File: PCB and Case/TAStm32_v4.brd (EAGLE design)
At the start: 50 x 100 mm, 47 parts, among them IC1 74AVCH4T245PW,118, IC2 74AVCH4T245PW,118, IC3 74AVCH4T245PW,118, J1 ZX62D-B-5PA8, J10 RJSSE538002, J11 RJSSE538002, J12 SOICBITE, J13 CONSOLE_RESET, J2 UE27-AC54-100, J3 TSM-105-02-L-SHJ, J4 CONSOLE_RESET, J5 OLED128X64, J6 SAMTEC-TSM-116-01-X-SVJ, J7 SAMTEC-TSM-116-01-X-SVJ, U1 STM32F446RET6, U2 3.3V REG, Y1 8MHz

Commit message: more new buffers
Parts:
- removed C15, C16, C19: 100nF, rcl:C0603K
- removed IC1, IC2, IC3: 74AVCH4T245PW,118, SamacSys_Parts:SOP65P640X110-16N
- removed RN3: CTS742C083, resistor-net:CTS742C083
- added IC4: 74LVC14, 74xx-us:SO14
- added IC5: 74HCT125, 74xx-eu:TSSOP14
- added IC7: 74LVC07, 74xx-us:SO14
- added RN4, RN5: CTS742C083, resistor-net:CTS742C083
- moved RN2 145.3 mm to (-9.75, -71.5)
- moved RN1 142.2 mm to (-9.75, -64.8)
- moved C13 132.5 mm to (-10.5, -54.7), turned to 0 degrees
- moved C14 126.5 mm to (-10.5, -59.1), turned to 0 degrees
- moved C5 123.6 mm to (-10.5, -50.3), turned to 0 degrees
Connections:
- removed net N$10: IC2.10, RN2.4
- removed net N$11: IC2.13, RN2.1
- removed net N$12: IC1.12, RN3.2
- removed net N$13: IC1.11, RN3.3
- removed net N$14: IC1.10, RN3.4
- removed net N$15: IC1.13, RN3.1
- removed net N$4: IC3.11, RN1.3
- removed net N$6: IC3.10, RN1.4
- removed net N$8: IC2.12, RN2.2
- removed net N$9: IC2.11, RN2.3
- removed net P1_5V: C13.2, C15.2, D1.A, IC1.16, IC3.16, J10.10, J6.10
- removed net P2_5V: C5.2, D2.A, IC2.16, J10.2, J6.2
- new net GND1: C13.1
- new net N$16: IC4.13, RN1.1, RN4.8
- new net N$17: IC4.11, RN1.2, RN4.7
- new net N$18: IC4.9, RN1.3, RN4.6
- new net N$21: IC4.5, RN2.3, RN5.6
- new net OUTPUTS_ENABLE: IC5.1, IC5.10, IC5.13, IC5.4
- new net P1_D2_3V_IN: IC4.8
- new net P1_VCC: D1.A, J10.10, J6.10
- new net P2_D3_3V_IN: IC4.6
- new net P2_VCC: D2.A, J10.2, J6.2
- new net V+1: C14.2, IC5.14
- net DIR_CLKLAT: no longer IC1.3, IC2.3
- net DIR_D0D1: no longer IC1.2, IC2.2
- net DIR_P1D2D3: no longer IC3.2
- net DIR_P2D2D3: no longer IC3.3
- net ENABLE_CLKLAT: no longer IC1.14, IC2.14
- net ENABLE_D0D1: no longer IC1.15, IC2.15
- net ENABLE_P1D2D3: no longer IC3.15
- net ENABLE_P2D2D3: no longer IC3.14
- net GND: now also IC4.7, IC5.7, IC7.11, IC7.13, IC7.7; no longer C13.1, C15.1, C16.1, C19.1, IC1.8, IC1.9, IC2.8, IC2.9, IC3.8, IC3.9
- net N$2: now also IC4.1, RN2.1, RN5.8; no longer IC3.13, RN1.1
- net N$3: now also IC4.3, RN2.2, RN5.7; no longer IC3.12, RN1.2
- net P1_CLOCK: now also RN4.2; no longer RN3.5
- net P1_CLOCK_3V: now also IC4.10; no longer IC1.7
- net P1_D0: now also IC5.3; no longer RN3.8
- net P1_D0_3V: now also IC5.2; no longer IC1.4
- net P1_D1: now also IC5.6; no longer RN3.7
- net P1_D1_3V: now also IC5.5; no longer IC1.5
- net P1_D2: now also IC7.2, RN4.3; no longer RN1.5
- net P1_D2_3V: now also IC7.1; no longer IC3.7
- net P1_D3: now also IC7.4; no longer RN1.6
- net P1_D3_3V: now also IC7.3; no longer IC3.6
- net P1_LATCH: now also RN4.1; no longer RN3.6
- net P1_LATCH_3V: now also IC4.12; no longer IC1.6
- net P2_CLOCK: now also RN5.2; no longer RN2.5
- net P2_CLOCK_3V: now also IC4.4; no longer IC2.7
- net P2_D0: now also IC5.8; no longer RN2.8
- net P2_D0_3V: now also IC5.9; no longer IC2.4
- net P2_D1: now also IC5.11; no longer RN2.7
- net P2_D1_3V: now also IC5.12; no longer IC2.5
- net P2_D2: now also IC7.6; no longer RN1.8
- net P2_D2_3V: now also IC7.5; no longer IC3.4
- net P2_D3: now also IC7.8, RN5.3; no longer RN1.7
- net P2_D3_3V: now also IC7.9; no longer IC3.5
- net P2_LATCH: now also RN5.1; no longer RN2.6
- net P2_LATCH_3V: now also IC4.2; no longer IC2.6
- net V+: now also C13.2, C5.2, IC4.14, IC7.14, RN1.6, RN1.7, RN1.8, RN2.6, RN2.7, RN2.8; no longer C14.2, C16.2, C19.2, IC1.1, IC2.1, IC3.1
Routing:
- net P1_5V: track 65.2 -> 0.00 mm, vias 4 -> 0
- net P1_VCC: track 0.00 -> 54.8 mm, vias 0 -> 2
- net P2_5V: track 51.7 -> 0.00 mm
- net P2_VCC: track 0.00 -> 43.6 mm
- net DIR_D0D1: track 39.5 -> 21.2 mm, vias 2 -> 0
- net DIR_CLKLAT: track 38.7 -> 21.5 mm
- net GND: track 134.3 -> 118.2 mm, vias 65 -> 52
- net V+: track 264.8 -> 258.0 mm
- net N$15: track 5.77 -> 0.00 mm
- net N$12: track 5.62 -> 0.00 mm
- net N$13: track 5.57 -> 0.00 mm
- net N$14: track 5.50 -> 0.00 mm
- net N$3: track 4.29 -> 0.00 mm
- net P2_CLOCK_3V: track 18.8 -> 14.7 mm
- net N$4: track 4.05 -> 0.00 mm
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
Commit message: bleh updates
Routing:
- net ENABLE_CLKLAT: track 47.0 -> 11.1 mm, vias 2 -> 0
- net V+: track 258.0 -> 228.0 mm, vias 13 -> 9
- net ENABLE_D0D1: track 42.1 -> 14.7 mm, vias 2 -> 0
- net ENABLE_P2D2D3: track 25.6 -> 8.01 mm, vias 2 -> 0
- net ENABLE_P1D2D3: track 25.7 -> 8.22 mm, vias 2 -> 0
- net P2_D3_3V: track 20.1 -> 8.42 mm
- net P1_D3_3V: track 18.9 -> 8.63 mm
- net P2_LATCH_3V: track 20.8 -> 12.0 mm, vias 2 -> 0
- net GND: track 118.2 -> 109.3 mm, vias 52 -> 40
- net DIR_P2D2D3: track 14.7 -> 6.36 mm
- net DIR_P1D2D3: track 14.2 -> 6.56 mm
- net P2_D0_3V: track 20.5 -> 13.0 mm, vias 2 -> 0
- net P2_D1_3V: track 19.0 -> 12.5 mm
- net P1_D2_3V: track 14.7 -> 8.84 mm
- net P2_CLOCK_3V: track 14.7 -> 9.07 mm, vias 2 -> 0
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
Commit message: more code work
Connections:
- net P2_D3_3V_IN renamed P2_D2_3V_IN
- net OUTPUTS_ENABLE: now also RN2.4
- net V+: now also RN2.5
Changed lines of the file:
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@@
 <contactref element="RN2" pad="7"/>
 <contactref element="RN2" pad="6"/>
+<contactref element="RN2" pad="5"/>
 <wire x1="-10.1536" y1="-70.6756" x2="-10.9536" y2="-70.6756" width="0" layer="19" extent="1-1"/>
 <wire x1="-9.3536" y1="-70.6756" x2="-10.1536" y2="-70.6756" width="0" layer="19" extent="1-1"/>
+<wire x1="-8.5536" y1="-70.6756" x2="-9.3536" y2="-70.6756" width="0" layer="19" extent="1-1"/>
 <wire x1="-10.9536" y1="-63.97" x2="-10.9536" y2="-70.6756" width="0" layer="19" extent="1-1"/>
 <wire x1="-10.1536" y1="-63.97" x2="-10.9536" y2="-63.97" width="0" layer="19" extent="1-1"/>
@@
 <contactref element="IC4" pad="8"/>
 </signal>
-<signal name="P2_D3_3V_IN">
+<signal name="P2_D2_3V_IN">
 <contactref element="IC4" pad="6"/>
 </signal>
@@
 <contactref element="IC5" pad="4"/>
 <contactref element="IC5" pad="1"/>
+<contactref element="RN2" pad="4"/>
+<wire x1="-9.2652" y1="-30.357" x2="-8.5536" y2="-72.2756" width="0" layer="19" extent="1-1"/>
 <wire x1="-7.3152" y1="-30.357" x2="-9.2652" y2="-30.357" width="0" layer="19" extent="1-1"/>
 <wire x1="-8.6152" y1="-24.507" x2="-9.2652" y2="-30.357" width="0" layer="19" extent="1-1"/>

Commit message: caps
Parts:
- added CN1, CN2: CA0612KRX7R7BB104, SamacSys_Parts:CA0612KRX7R7BB104
- added RN3: CTS742C083, resistor-net:CTS742C083
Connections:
- removed net N$21: IC4.5, RN2.3, RN5.6
- new net N$4: CN2.8, IC4.1, RN2.1, RN5.8
- new net N$6: CN2.7, IC4.3, RN2.2, RN5.7
- new net N$8: CN2.6, IC4.5, RN2.3, RN5.6
- net GND: now also CN1.1, CN1.2, CN1.3, CN1.4, CN2.1, CN2.2, CN2.3, CN2.4
- net N$16: now also CN1.8
- net N$17: now also CN1.7
- net N$18: now also CN1.6
- net N$2: now also IC5.6, RN3.2; no longer IC4.1, RN2.1, RN5.8
- net N$3: now also IC5.3, RN3.1; no longer IC4.3, RN2.2, RN5.7
- net P1_D0: now also RN3.8; no longer IC5.3
- net P1_D1: now also RN3.7; no longer IC5.6
- net P1_D2: now also RN3.6; no longer IC7.2
- net P1_D3: now also RN3.5; no longer IC7.4

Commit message: new new new new buffers
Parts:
- removed IC5: 74HCT125, 74xx-eu:TSSOP14
- removed IC7: 74LVC07, 74xx-us:SO14
- added C15, C16, C17: 100nF, rcl:C0603K
- added CN3, CN4: CA0612KRX7R7BB104, SamacSys_Parts:CA0612KRX7R7BB104
- added IC1, IC2: 74HCT3G07DP-Q100H, SamacSys_Parts:SOP65P400X110-8N
- added IC3: 74AVCH4T245PW,118, SamacSys_Parts:SOP65P640X110-16N
- added RN7: CTS742C083, resistor-net:CTS742C083
- IC4: value 74LVC14 -> 74AVCH4T245PW,118; device 74xx-us:SO14 -> SamacSys_Parts:SOP65P640X110-16N
- moved RN3 170.9 mm to (53.8, 68.4)
- moved CN2 161.5 mm to (53.5, 67.5), turned to 90 degrees
- moved RN1 154.2 mm to (57.5, 74.1)
- moved C5 152.1 mm to (58.1, 85.5)
- moved RN2 144.4 mm to (38.6, 64.6)
- moved CN1 143.9 mm to (47.7, 61.9), turned to 270 degrees
- moved C13 143.5 mm to (62.9, 68.6)
- moved C14 143.5 mm to (62.9, 64.2)
- moved RN5 97.1 mm to (42.8, 62.0)
- moved RN4 94.0 mm to (38.4, 67.8)
- moved IC4 74.7 mm to (32.5, 59.0), turned to 90 degrees
- moved C3 2.12 mm to (47.2, 36.0)
- moved C1 2.00 mm to (35.0, 45.9)
- moved C11 2.00 mm to (45.8, 40.3)
- moved C12 2.00 mm to (45.8, 42.1)
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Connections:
- removed net DIR_CLKLAT: U1.14
- removed net ENABLE_CLKLAT: U1.29
- removed net GND1: C13.1
- removed net OUTPUTS_ENABLE: IC5.1, IC5.10, IC5.13, IC5.4, RN2.4
- removed net P1_D2_3V: IC7.1, U1.24
- removed net P2_D2_3V: IC7.5, U1.40
- removed net V+1: C14.2, IC5.14
- new net N$10: IC3.10, RN3.4
- new net N$11: IC4.12, RN7.2
- new net N$12: IC4.13, RN7.1
- new net N$13: IC4.11, RN7.3
- new net N$14: IC4.10, RN7.4
- new net N$9: IC3.11, RN3.3
- new net P1_D2_3V_OUT: IC3.4, U1.15
- new net P2_D2_3V_OUT: IC4.6
- net DIR_D0D1: now also IC3.3, IC4.2, U1.16; no longer U1.15
- net DIR_P1D2D3: now also IC3.2, U1.20; no longer U1.27
- net DIR_P2D2D3: now also IC4.3
- net ENABLE_D0D1: now also IC3.14, IC4.15, U1.21; no longer U1.16
- net ENABLE_P1D2D3: now also IC3.15, U1.22; no longer U1.21
- net ENABLE_P2D2D3: now also IC4.14; no longer U1.20
- net GND: now also C13.2, C15.2, C16.1, C17.2, C5.2, CN3.1, CN3.2, CN3.3, CN3.4, CN4.1, CN4.2, CN4.3, CN4.4, IC1.4, IC2.4, IC3.8, IC3.9, IC4.8, IC4.9; no longer C5.1, IC4.7, IC5.7, IC7.11, IC7.13, IC7.7
- net N$16: now also IC1.1; no longer IC4.13
- net N$17: now also IC1.6; no longer IC4.11
- net N$18: now also IC1.3; no longer IC4.9
- net N$2: now also IC3.12; no longer IC5.6
- net N$3: now also IC3.13; no longer IC5.3
- net N$4: now also IC2.1; no longer IC4.1
- net N$6: now also IC2.6; no longer IC4.3
- net N$8: now also IC2.3; no longer IC4.5
- net P1_CLOCK_3V: now also IC1.2; no longer IC4.10
- net P1_D0: now also CN3.8
- net P1_D0_3V: now also IC3.6; no longer IC5.2
- net P1_D1: now also CN3.5
- net P1_D1_3V: now also IC3.7; no longer IC5.5
- net P1_D2_3V_IN: now also IC1.5, U1.24; no longer IC4.8
- net P1_D3_3V: now also IC3.5, U1.14; no longer IC7.3
- net P1_LATCH_3V: now also IC1.7; no longer IC4.12
- net P1_VCC: now also C15.1, C17.1, IC3.16, IC4.16
- net P2_CLOCK_3V: now also IC2.2; no longer IC4.4
- net P2_D0: now also CN4.5, RN7.7; no longer IC5.8
- net P2_D0_3V: now also IC4.5; no longer IC5.9
- net P2_D1: now also CN4.8, RN7.8; no longer IC5.11
- net P2_D1_3V: now also IC4.4; no longer IC5.12
- net P2_D2: now also RN5.3, RN7.6; no longer IC7.6
- net P2_D2_3V_IN: now also IC2.5, U1.40; no longer IC4.6
- net P2_D3: now also RN7.5; no longer IC7.8, RN5.3
- net P2_D3_3V: now also IC4.7, U1.27; no longer IC7.9, U1.22
- net P2_LATCH_3V: now also IC2.7; no longer IC4.2
- net V+: now also C13.1, C14.2, C16.2, C5.1, IC1.8, IC2.8, IC3.1, IC4.1; no longer C13.2, C5.2, IC4.14, IC7.14
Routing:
- net P2_LATCH_3V: track 12.0 -> 33.1 mm
- net P2_D2_3V: track 20.0 -> 0.00 mm, vias 2 -> 0
- net SWITCH3: track 23.8 -> 5.94 mm
- net P1_D3_3V: track 8.63 -> 25.9 mm
- net P1_D2_3V_OUT: track 0.00 -> 16.8 mm
- net DIR_CLKLAT: track 16.5 -> 0.00 mm
- net DIR_P2D2D3: track 6.36 -> 22.5 mm
- net P2_D2_3V_IN: track 0.00 -> 11.2 mm
- net ENABLE_CLKLAT: track 11.1 -> 0.00 mm
- net ENABLE_P1D2D3: track 8.22 -> 18.3 mm
- net P1_D2_3V_IN: track 0.00 -> 8.84 mm
- net P1_D2_3V: track 8.84 -> 0.00 mm
- net P2_D1_3V: track 12.5 -> 20.8 mm
- net P2_D0_3V: track 13.0 -> 21.2 mm
- net P2_D3_3V: track 8.42 -> 15.8 mm
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
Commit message: new buffer funtimes
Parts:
- moved C16 35.1 mm to (41.3, 50.1), turned to 90 degrees
- moved C13 26.9 mm to (37.9, 58.5)
- moved C15 22.0 mm to (41.0, 61.6), turned to 90 degrees
- moved C14 19.5 mm to (47.7, 52.0)
- moved RN1 16.2 mm to (47.9, 61.0)
- moved CN2 15.7 mm to (38.0, 65.0), turned to 270 degrees
- moved RN3 12.3 mm to (43.6, 61.6)
- moved CN3 11.4 mm to (43.6, 65.1), turned to 270 degrees
- moved CN4 9.84 mm to (33.1, 68.6), turned to 270 degrees
- moved RN4 9.33 mm to (47.7, 68.6), turned to 180 degrees
- moved RN5 7.92 mm to (38.0, 68.3), turned to 180 degrees
- moved RN2 3.12 mm to (38.0, 61.5)
- moved CN1 2.74 mm to (47.7, 64.6)
- moved IC2 1.07 mm to (38.0, 54.9)
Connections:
- net N$16: now also RN1.3; no longer RN1.1
- net N$17: now also RN1.1; no longer RN1.2
- net N$18: now also RN1.2; no longer RN1.3
- net N$4: now also CN2.6, RN2.2, RN5.6; no longer CN2.8, RN2.1, RN5.8
- net N$6: now also CN2.5, RN2.1, RN5.5; no longer CN2.7, RN2.2, RN5.7
- net N$8: now also CN2.8, RN2.4, RN5.8; no longer CN2.6, RN2.3, RN5.6
- net P1_D0: now also CN3.7, RN3.6; no longer CN3.8, RN3.8
- net P1_D1: now also CN3.8, RN3.5; no longer CN3.5, RN3.7
- net P1_D2: now also RN3.8; no longer RN3.6
- net P1_D3: now also RN3.7; no longer RN3.5
- net P1_D3_3V: no longer U1.23
- net P1_VCC: no longer C17.1, IC4.16
- net P2_D0: now also CN4.8; no longer CN4.5
- net P2_D1: now also CN4.5; no longer CN4.8
- net P2_VCC: now also C17.1, IC4.16
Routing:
- net N$4: track 0.00 -> 22.0 mm
- net P2_D2_3V_IN: track 11.2 -> 28.9 mm, vias 0 -> 2
- net N$8: track 0.00 -> 17.0 mm
- net P2_D0: track 30.0 -> 45.9 mm
- net N$6: track 0.00 -> 13.8 mm
- net P1_VCC: track 51.3 -> 37.7 mm, vias 2 -> 0
- net P1_D2_3V_IN: track 8.84 -> 22.3 mm, vias 0 -> 2
- net P1_D0: track 18.4 -> 27.3 mm
- net P1_D3_3V: track 25.9 -> 17.3 mm
- net P1_D1: track 18.3 -> 26.8 mm
- net P1_D2: track 19.6 -> 27.9 mm
- net P2_LATCH: track 25.7 -> 33.6 mm, vias 0 -> 2
- net P2_LATCH_3V: track 33.1 -> 25.7 mm
- net V+: track 221.2 -> 227.7 mm
- net P1_LATCH: track 17.6 -> 11.4 mm
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
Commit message: no airwires!
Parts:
- CN1, CN2, CN3, CN4: value CA0612KRX7R7BB104 -> 330pF
- RN1, RN2, RN5: value CTS742C083 -> 47K
- RN4, RN7: value CTS742C083 -> 47R
- moved C5 40.8 mm to (31.2, 54.7)
- moved C17 35.9 mm to (30.2, 65.2), turned to 90 degrees
- moved RN5 0.61 mm to (38.0, 68.9)
- moved IC4 0.55 mm to (33.0, 59.3)
- moved CN3 0.46 mm to (43.1, 65.1)
- moved C14 0.34 mm to (47.4, 51.8)
- moved IC1 0.30 mm to (47.7, 56.0)
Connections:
- removed net N$13: IC4.11, RN7.3
- removed net N$14: IC4.10, RN7.4
- removed net N$2: IC3.12, RN3.2
- removed net N$3: IC3.13, RN3.1
- net ENABLE_P2D2D3: now also U1.23
- net N$16: now also CN1.7, RN4.7; no longer CN1.8, RN4.8
- net N$17: now also CN1.5, RN4.5; no longer CN1.7, RN4.7
- net P1_CLOCK: now also RN4.4; no longer RN4.2
- net P1_D2: now also IC3.13, RN3.1
- net P1_D3: now also IC3.12, RN3.2
- net P1_LATCH: now also RN4.2; no longer RN4.1
- net P1_VCC: now also RN1.5, RN1.6, RN1.7, RN1.8
- net P2_CLOCK: now also RN5.4; no longer RN5.2
- net P2_D2: now also IC4.11, RN5.1, RN7.3; no longer RN5.3
- net P2_D2_3V_OUT: now also U1.29
- net P2_D3: now also IC4.10, RN7.4
- net P2_LATCH: now also RN5.3; no longer RN5.1
- net P2_VCC: now also RN2.5, RN2.6, RN2.7, RN2.8
- net V+: no longer RN1.6, RN1.7, RN1.8, RN2.5, RN2.6, RN2.7, RN2.8
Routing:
- net V+: track 227.7 -> 281.0 mm, vias 9 -> 15
- net P1_VCC: track 37.7 -> 84.0 mm, vias 0 -> 4
- net P1_D2: track 27.9 -> 59.1 mm
- net GND: track 103.1 -> 133.7 mm, vias 34 -> 52
- net P1_LATCH: track 11.4 -> 38.5 mm
- net P2_VCC: track 43.6 -> 68.6 mm, vias 0 -> 2
- net ENABLE_P2D2D3: track 4.90 -> 27.4 mm, vias 0 -> 4
- net DIR_D0D1: track 16.2 -> 38.4 mm, vias 0 -> 4
- net SWITCH3: track 5.94 -> 23.3 mm
- net P2_D2_3V_OUT: track 0.00 -> 17.0 mm
- net ENABLE_D0D1: track 18.3 -> 34.0 mm, vias 0 -> 2
- net NRST: track 68.0 -> 82.8 mm, vias 2 -> 4
- net N$16: track 2.48 -> 14.3 mm
- net N$18: track 2.28 -> 13.9 mm
- net P2_D2: track 43.0 -> 54.3 mm, vias 0 -> 2
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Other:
- board text added: "TAStm32"
- board text added: "v4 rev2"
- board text removed: "TAStm32 v4 rev2"

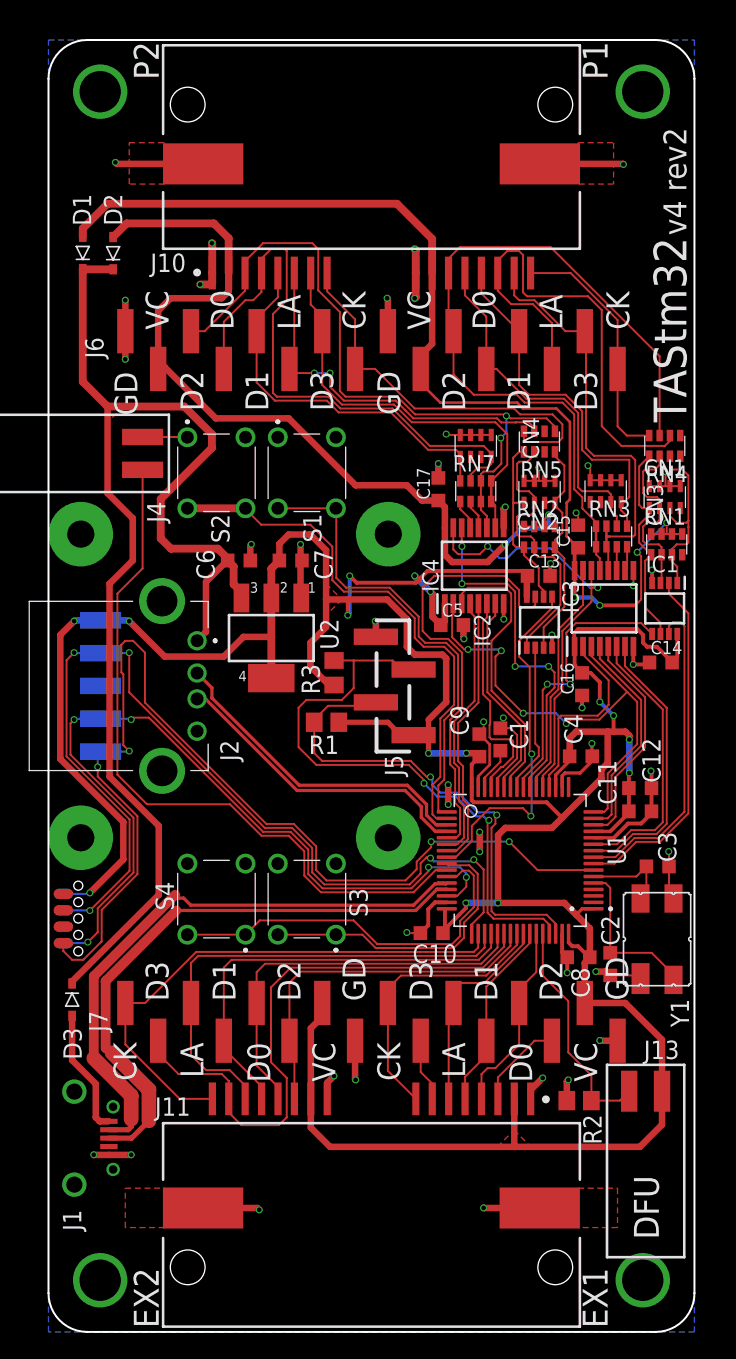
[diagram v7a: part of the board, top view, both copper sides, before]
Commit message: v4 r2 silkscreen cleanup, combi vis board
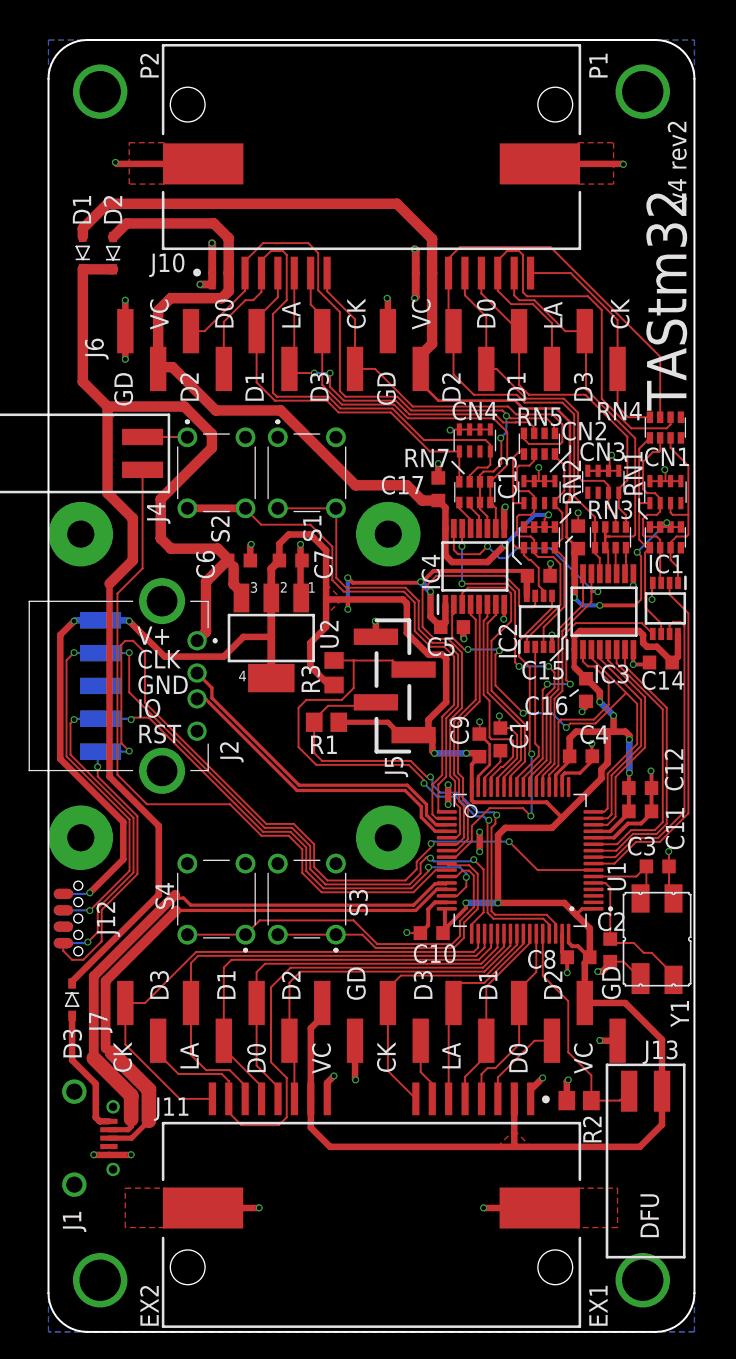
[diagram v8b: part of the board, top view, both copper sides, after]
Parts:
- moved RN4 1.42 mm to (47.8, 70.0)
- moved C2 1.07 mm to (43.5, 29.5)
- moved CN3 0.75 mm to (42.9, 65.8)
- moved RN1 0.55 mm to (47.8, 61.5)
- moved C16 0.55 mm to (41.6, 49.7)
- moved CN4 0.43 mm to (33.0, 69.0)
- moved CN1 0.39 mm to (47.8, 65.0)
- moved IC3 0.25 mm to (43.0, 55.8)
- moved RN5 0.16 mm to (38.0, 68.8)
- moved C5 0.15 mm to (31.2, 54.6)
- moved RN3 0.11 mm to (43.5, 61.5)
- moved RN7 0.10 mm to (33.0, 65.0)
- moved C15 0.07 mm to (41.0, 61.5)
- moved IC4 0.07 mm to (33.0, 59.2)
- moved IC2 0.07 mm to (38.0, 55.0)
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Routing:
- net V+: track 281.0 -> 278.3 mm
- net P1_LATCH: track 38.5 -> 36.9 mm
- net P1_CLOCK: track 19.2 -> 17.8 mm
- net P1_D3: track 33.2 -> 31.8 mm
- net N$17: track 16.1 -> 17.5 mm
- net GND: track 133.7 -> 134.8 mm
- net N$18: track 13.9 -> 15.1 mm
- net P1_D2: track 59.1 -> 57.9 mm
- net N$16: track 14.3 -> 15.2 mm
- net P1_D1: track 28.3 -> 27.4 mm
- net XTAL1: track 12.5 -> 11.9 mm
- net P1_VCC: track 84.0 -> 83.5 mm
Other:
- board text added: "CLK"
- board text added: "GND"
- board text added: "IO"
- board text added: "RST"
- board text added: "V+"
